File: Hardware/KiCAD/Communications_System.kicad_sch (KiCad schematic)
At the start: 19 parts, among them IC2 CC1200RHBR, Y1 40 MHz

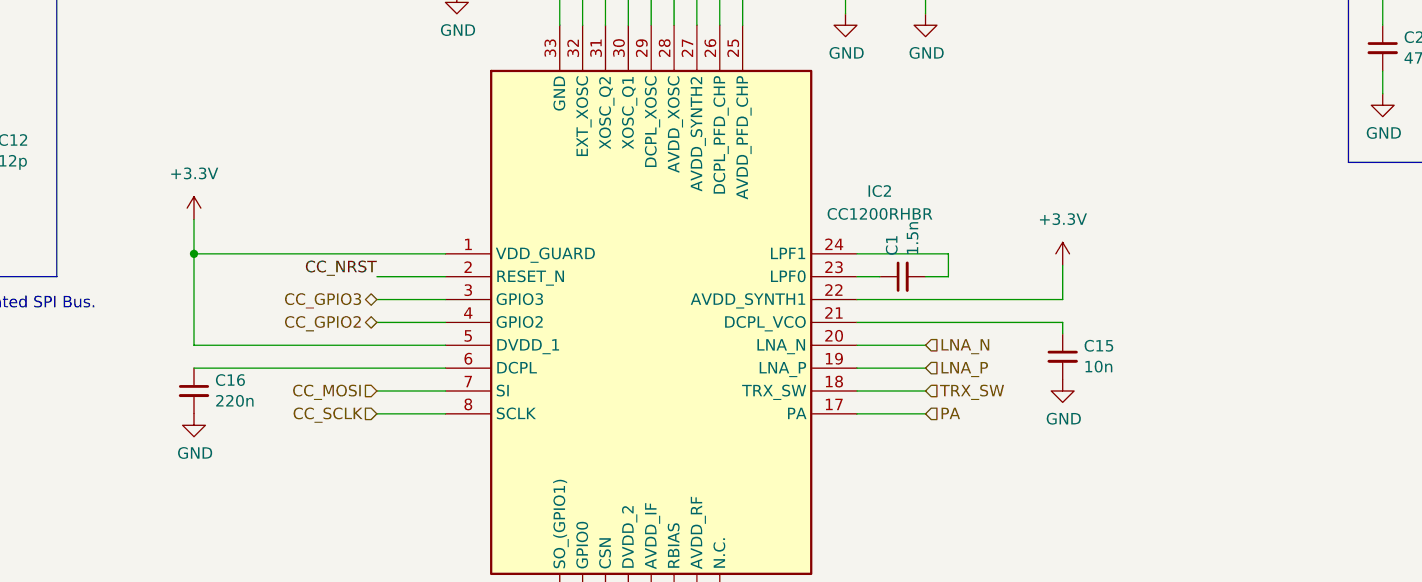
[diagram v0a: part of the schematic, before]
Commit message: Added seperate schematic for amplifier assembly
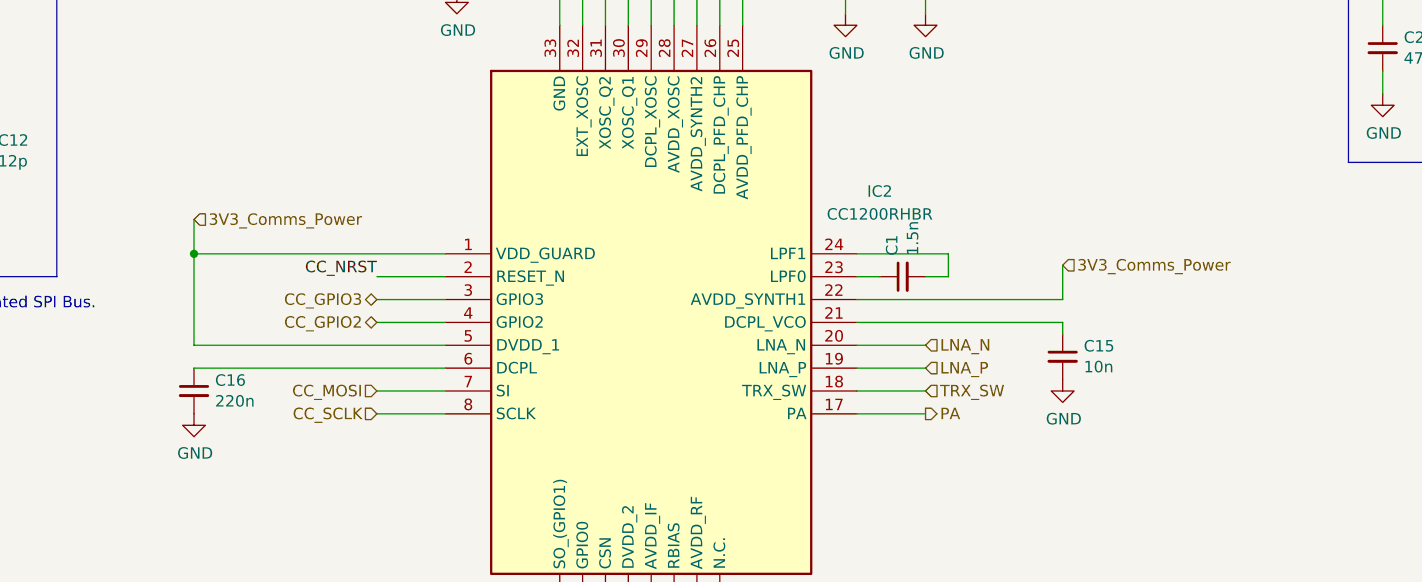
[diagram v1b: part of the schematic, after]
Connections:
- net +3.3V is gone; now on net 3V3_Comms_Power: IC2.1 (VDD_GUARD), IC2.22 (AVDD_SYNTH1), IC2.5 (DVDD_1)
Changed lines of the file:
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@@
     (effects (font (size 1.27 1.27)) (justify right))
+  )
+  (hierarchical_label "3V3_Comms_Power" (shape input) (at 64.77 55.88 0) (fields_autoplaced)
+    (effects (font (size 1.27 1.27)) (justify left))
   )
   (hierarchical_label "3V3_Comms_Power" (shape input) (at 196.85 22.86 0) (fields_autoplaced)
@@
     (effects (font (size 1.27 1.27)) (justify left))
   )
-  (hierarchical_label "PA" (shape input) (at 146.05 77.47 0) (fields_autoplaced)
+  (hierarchical_label "PA" (shape output) (at 146.05 77.47 0) (fields_autoplaced)
+    (effects (font (size 1.27 1.27)) (justify left))
+  )
+  (hierarchical_label "3V3_Comms_Power" (shape input) (at 161.29 60.96 0) (fields_autoplaced)
     (effects (font (size 1.27 1.27)) (justify left))
   )
@@
         (path "/c89c6552-5574-4959-bcaf-f05dfde21961/f4521ef1-9a41-474d-b880-30e1e54c8ecb"
           (reference "#PWR034") (unit 1)
-        )
-      )
-    )
-  )
-  (symbol (lib_id "power:+3.3V") (at 161.29 60.96 0) (unit 1)
-    (in_bom yes) (on_board yes) (dnp no) (fields_autoplaced)
-    (property "Reference" "#PWR025" (at 161.29 64.77 0)
-      (effects (font (size 1.27 1.27)) hide)
-    )
-    (property "Value" "+3.3V" (at 161.29 55.88 0)
-      (effects (font (size 1.27 1.27)))
-    )
-    (property "Footprint" "" (at 161.29 60.96 0)
-      (effects (font (size 1.27 1.27)) hide)
-    )
-    (property "Datasheet" "" (at 161.29 60.96 0)
-      (effects (font (size 1.27 1.27)) hide)
-    )
-    (pin "1")
-    (instances
-      (project "Cobalt-Cowboy"
-        (path "/60a68eb1-aa0f-414e-b03b-965ad6b52dab/1039084b-a0e1-47ac-823b-a237cfc3ed39"
-          (reference "#PWR025") (unit 1)
-        )
-        (path "/60a68eb1-aa0f-414e-b03b-965ad6b52dab/d80d452c-0cd9-4253-b692-c2cdb4b1394b"
-          (reference "#PWR021") (unit 1)
         )
       )
@@
         )
       )
-    )
-  )
-  (symbol (lib_id "power:+3.3V") (at 64.77 55.88 0) (unit 1)
-    (in_bom yes) (on_board yes) (dnp no) (fields_autoplaced)
-    (property "Reference" "#PWR025" (at 64.77 59.69 0)
-      (effects (font (size 1.27 1.27)) hide)
-    )
-    (property "Value" "+3.3V" (at 64.77 50.8 0)
-      (effects (font (size 1.27 1.27)))
-    )
-    (property "Footprint" "" (at 64.77 55.88 0)
-      (effects (font (size 1.27 1.27)) hide)
-    )
-    (property "Datasheet" "" (at 64.77 55.88 0)
-      (effects (font (size 1.27 1.27)) hide)
-    )
-    (pin "1")
-    (instances
-      (project "Cobalt-Cowboy"
-        (path "/60a68eb1-aa0f-414e-b03b-965ad6b52dab/1039084b-a0e1-47ac-823b-a237cfc3ed39"
-          (reference "#PWR025") (unit 1)
-        )
-        (path "/60a68eb1-aa0f-414e-b03b-965ad6b52dab/d80d452c-0cd9-4253-b692-c2cdb4b1394b"
-          (reference "#PWR023") (unit 1)
-        )
-      )

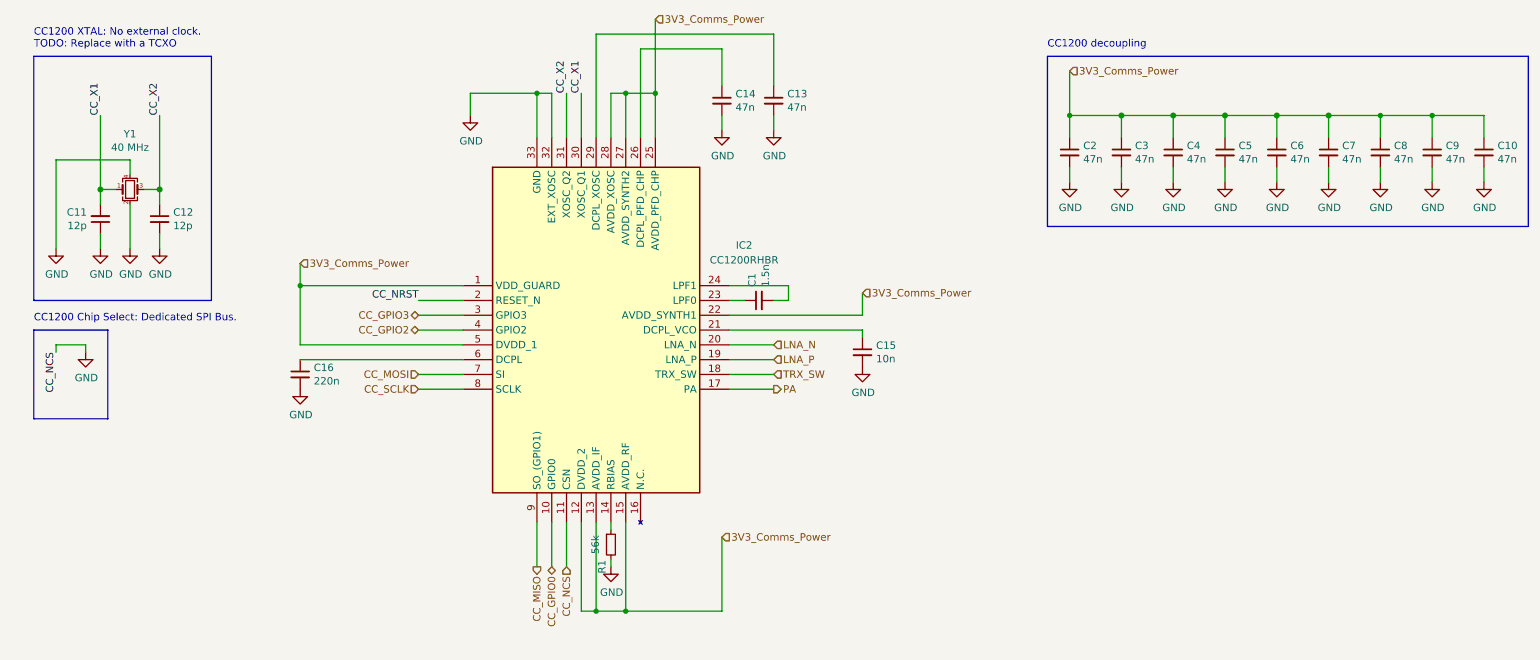
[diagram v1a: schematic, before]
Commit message: feat: subsystem exploration, begin placement, routing #11 #12 #4 many new project symbols
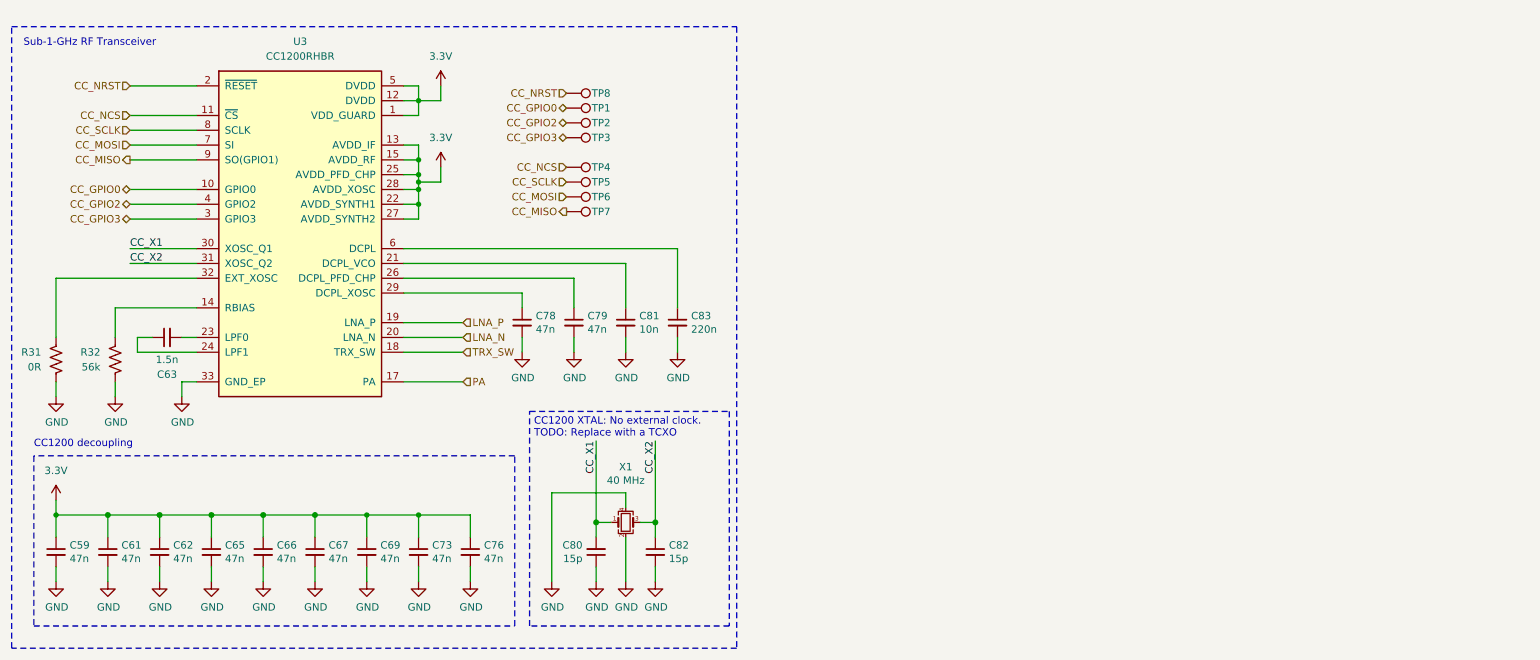
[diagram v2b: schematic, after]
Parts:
- removed C1: 1.5n, Capacitor_SMD:C_0402_1005Metric, symbol pkl_device:pkl_C_Small
- removed C10, C13, C14, C2, C3, C4, C5, C6, C7, C8, C9: 47n, Capacitor_SMD:C_0402_1005Metric, symbol pkl_device:pkl_C_Small
- removed C11, C12: 12p, Capacitor_SMD:C_0402_1005Metric, symbol pkl_device:pkl_C_Small
- removed C15: 10n, Capacitor_SMD:C_0402_1005Metric, symbol pkl_device:pkl_C_Small
- removed C16: 220n, Capacitor_SMD:C_0402_1005Metric, symbol pkl_device:pkl_C_Small
- removed IC2: CC1200RHBR, Cobalt_Cowboy:QFN50P500X500X100-33N-D, symbol Cobalt_Cowboy:CC1200RHBR
- removed R1: 56k, Resistor_SMD:R_0402_1005Metric, symbol pkl_device:pkl_R_Small
- removed Y1: 40 MHz, Crystal:Crystal_SMD_3225-4Pin_3.2x2.5mm, symbol Device:Crystal_GND24_Small
- added C59, C61, C62, C65, C66, C67, C69, C73, C76, C78, C79: 47n, Capacitor_SMD:C_0402_1005Metric, symbol Device:C_Small
- added C63: 1.5n, Capacitor_SMD:C_0402_1005Metric, symbol Device:C_Small
- added C80, C82: 15p, Capacitor_SMD:C_0402_1005Metric, symbol Device:C_Small
- added C81: 10n, Capacitor_SMD:C_0402_1005Metric, symbol Device:C_Small
- added C83: 220n, Capacitor_SMD:C_0402_1005Metric, symbol Device:C_Small
- added R31: 0R, Resistor_SMD:R_0402_1005Metric, symbol Device:R_US
- added R32: 56k, Resistor_SMD:R_0402_1005Metric, symbol Device:R_US
- added TP1, TP2, TP3, TP4, TP5, TP6, TP7, TP8: TestPoint, TestPoint:TestPoint_Pad_D1.0mm, symbol Connector:TestPoint
- added U3: CC1200RHBR, Package_DFN_QFN:QFN-32-1EP_5x5mm_P0.5mm_EP3.45x3.45mm, symbol RF:CC1200
- added X1: 40 MHz, Crystal:Crystal_SMD_3225-4Pin_3.2x2.5mm, symbol Device:Crystal_GND24_Small
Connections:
- net CC_GPIO0: now also TP1.1, U3.10 (GPIO0)
- net CC_GPIO2: now also TP2.1, U3.4 (GPIO2)
- net CC_GPIO3: now also TP3.1, U3.3 (GPIO3)
- net CC_MISO: now also TP7.1, U3.9 (SO(GPIO1))
- net CC_MOSI: now also TP6.1, U3.7 (SI)
- net CC_NRST: now also TP8.1, U3.2 (~{RESET})
- net CC_SCLK: now also TP5.1, U3.8 (SCLK)
- net CC_X1: now also C80.2, U3.30 (XOSC_Q1), X1.1
- net CC_X2: now also C82.1, U3.31 (XOSC_Q2), X1.3
- net GND: now also C59.2, C61.2, C62.2, C65.2, C66.2, C67.2, C69.2, C73.2, C76.2, C78.2, C79.2, C80.1, C81.2, C82.2, C83.2, R31.1, R32.2, U3.33 (GND_EP), X1.2, X1.4
- net LNA_N: now also U3.20 (LNA_N)
- net LNA_P: now also U3.19 (LNA_P)
- net PA: now also U3.17 (PA)
- net TRX_SW: now also U3.18 (TRX_SW)
- new net: R32.1, U3.14 (RBIAS)
- new net: C81.1, U3.21 (DCPL_VCO)
- new net: C63.2, U3.23 (LPF0)
- new net: C63.1, U3.24 (LPF1)
- new net: C79.1, U3.26 (DCPL_PFD_CHP)
- new net: C78.1, U3.29 (DCPL_XOSC)
- new net: R31.2, U3.32 (EXT_XOSC)
- new net: C83.1, U3.6 (DCPL)
- new net 3.3V: C59.1, C61.1, C62.1, C65.1, C66.1, C67.1, C69.1, C73.1, C76.1, U3.1 (VDD_GUARD), U3.12 (DVDD), U3.13 (AVDD_IF), U3.15 (AVDD_RF), U3.22 (AVDD_SYNTH1), U3.25 (AVDD_PFD_CHP), U3.27 (AVDD_SYNTH2), U3.28 (AVDD_XOSC), U3.5 (DVDD)
- new net CC_NCS: TP4.1, U3.11 (~{CS})
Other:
- note added: "Sub-1-GHz RF Transceiver"
- note removed: "CC1200 Chip Select: Dedicated SPI Bus."
